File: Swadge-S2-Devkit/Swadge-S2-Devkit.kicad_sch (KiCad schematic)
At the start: 90 parts, among them J2 DEBUG_BANK_C, J3 DEBUG_BANK_B, J4 DEBUG_BANK_A, J5 MICSEL, J6 TRYMIC, M1 Motor_DC, Q1 Q_N_FET, Q2 AP2003_PN_FET, Q3 AP2003_PN_FET, Q4 AP2003_PN_FET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

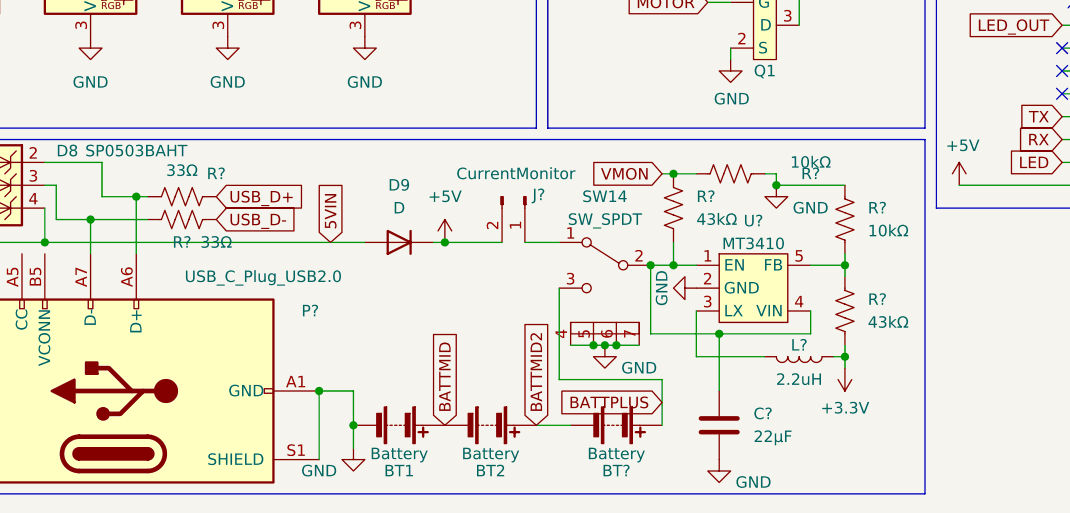
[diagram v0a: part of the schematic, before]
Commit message: Added annotated schematic
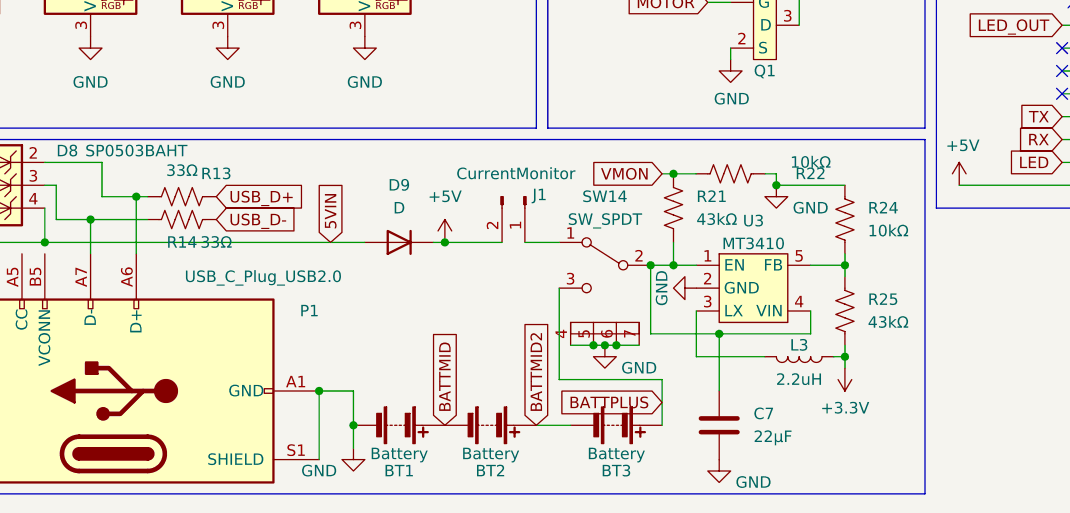
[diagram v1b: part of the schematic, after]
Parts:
- gave numbers to parts that had none: 12
